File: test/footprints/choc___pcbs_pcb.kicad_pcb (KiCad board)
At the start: 2 copper layers, 5 parts

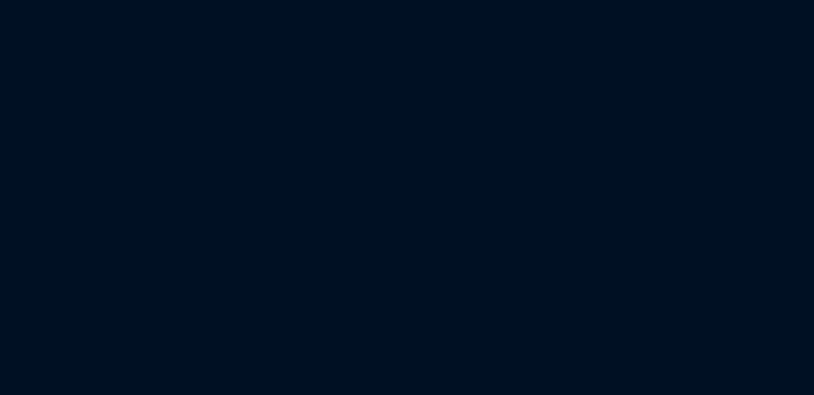
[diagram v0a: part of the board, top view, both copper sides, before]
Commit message: expand code coverage for `choc` footprint
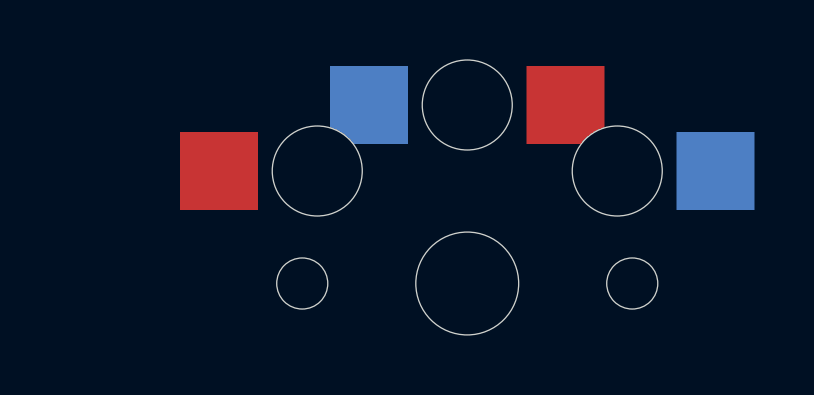
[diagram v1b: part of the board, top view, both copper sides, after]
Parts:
- added S6: , PG1350, F.Cu at (250.0, 0.00)
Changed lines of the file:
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@@
+          (pad 2 smd rect (at -8.275 -3.75 0) (size 2.6 2.6) (layers F.Cu F.Paste F.Mask)  (net 2 "to"))
+        )
+      (module PG1350 (layer F.Cu)
+      (at 250 0 0)
+      (fp_text reference "S6" (at 0 0) (layer F.SilkS) hide (effects (font (size 1.27 1.27) (thickness 0.15))))
+      (fp_text value "" (at 0 0) (layer F.SilkS) hide (effects (font (size 1.27 1.27) (thickness 0.15))))
+      (fp_line (start -7 -6) (end -7 -7) (layer Dwgs.User) (width 0.15))
+      (fp_line (start -7 7) (end -6 7) (layer Dwgs.User) (width 0.15))
+      (fp_line (start -6 -7) (end -7 -7) (layer Dwgs.User) (width 0.15))
+      (fp_line (start -7 7) (end -7 6) (layer Dwgs.User) (width 0.15))
+      (fp_line (start 7 6) (end 7 7) (layer Dwgs.User) (width 0.15))
+      (fp_line (start 7 -7) (end 6 -7) (layer Dwgs.User) (width 0.15))
+      (fp_line (start 6 7) (end 7 7) (layer Dwgs.User) (width 0.15))
+      (fp_line (start 7 -7) (end 7 -6) (layer Dwgs.User) (width 0.15))
+      (pad "" np_thru_hole circle (at 0 0) (size 3.429 3.429) (drill 3.429) (layers *.Cu *.Mask))
+      (pad "" np_thru_hole circle (at 5.5 0) (size 1.7018 1.7018) (drill 1.7018) (layers *.Cu *.Mask))
+      (pad "" np_thru_hole circle (at -5.5 0) (size 1.7018 1.7018) (drill 1.7018) (layers *.Cu *.Mask))
+      (fp_line (start -9 -8.5) (end 9 -8.5) (layer Dwgs.User) (width 0.15))
+      (fp_line (start 9 -8.5) (end 9 8.5) (layer Dwgs.User) (width 0.15))
+      (fp_line (start 9 8.5) (end -9 8.5) (layer Dwgs.User) (width 0.15))
+      (fp_line (start -9 8.5) (end -9 -8.5) (layer Dwgs.User) (width 0.15))
+          (pad "" np_thru_hole circle (at 5 -3.75) (size 3 3) (drill 3) (layers *.Cu *.Mask))
+          (pad "" np_thru_hole circle (at 0 -5.95) (size 3 3) (drill 3) (layers *.Cu *.Mask))
+          (pad 1 smd rect (at -3.275 -5.95 0) (size 2.6 2.6) (layers B.Cu B.Paste B.Mask)  (net 1 "from"))
+          (pad 2 smd rect (at 8.275 -3.75 0) (size 2.6 2.6) (layers B.Cu B.Paste B.Mask)  (net 2 "to"))
+          (pad "" np_thru_hole circle (at -5 -3.75) (size 3 3) (drill 3) (layers *.Cu *.Mask))
+          (pad "" np_thru_hole circle (at 0 -5.95) (size 3 3) (drill 3) (layers *.Cu *.Mask))
+          (pad 1 smd rect (at 3.275 -5.95 0) (size 2.6 2.6) (layers F.Cu F.Paste F.Mask)  (net 1 "from"))
           (pad 2 smd rect (at -8.275 -3.75 0) (size 2.6 2.6) (layers F.Cu F.Paste F.Mask)  (net 2 "to"))
         )
